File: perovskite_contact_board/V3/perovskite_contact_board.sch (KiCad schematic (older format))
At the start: 39 parts, among them U1 Perovskite_CP_6_Cell, U2 Perovskite_CP_6_Cell, U3 Perovskite_CP_6_Cell, U4 MCP9808_MSOP, U5 MCP9808_MSOP, U6 MCP9808_MSOP

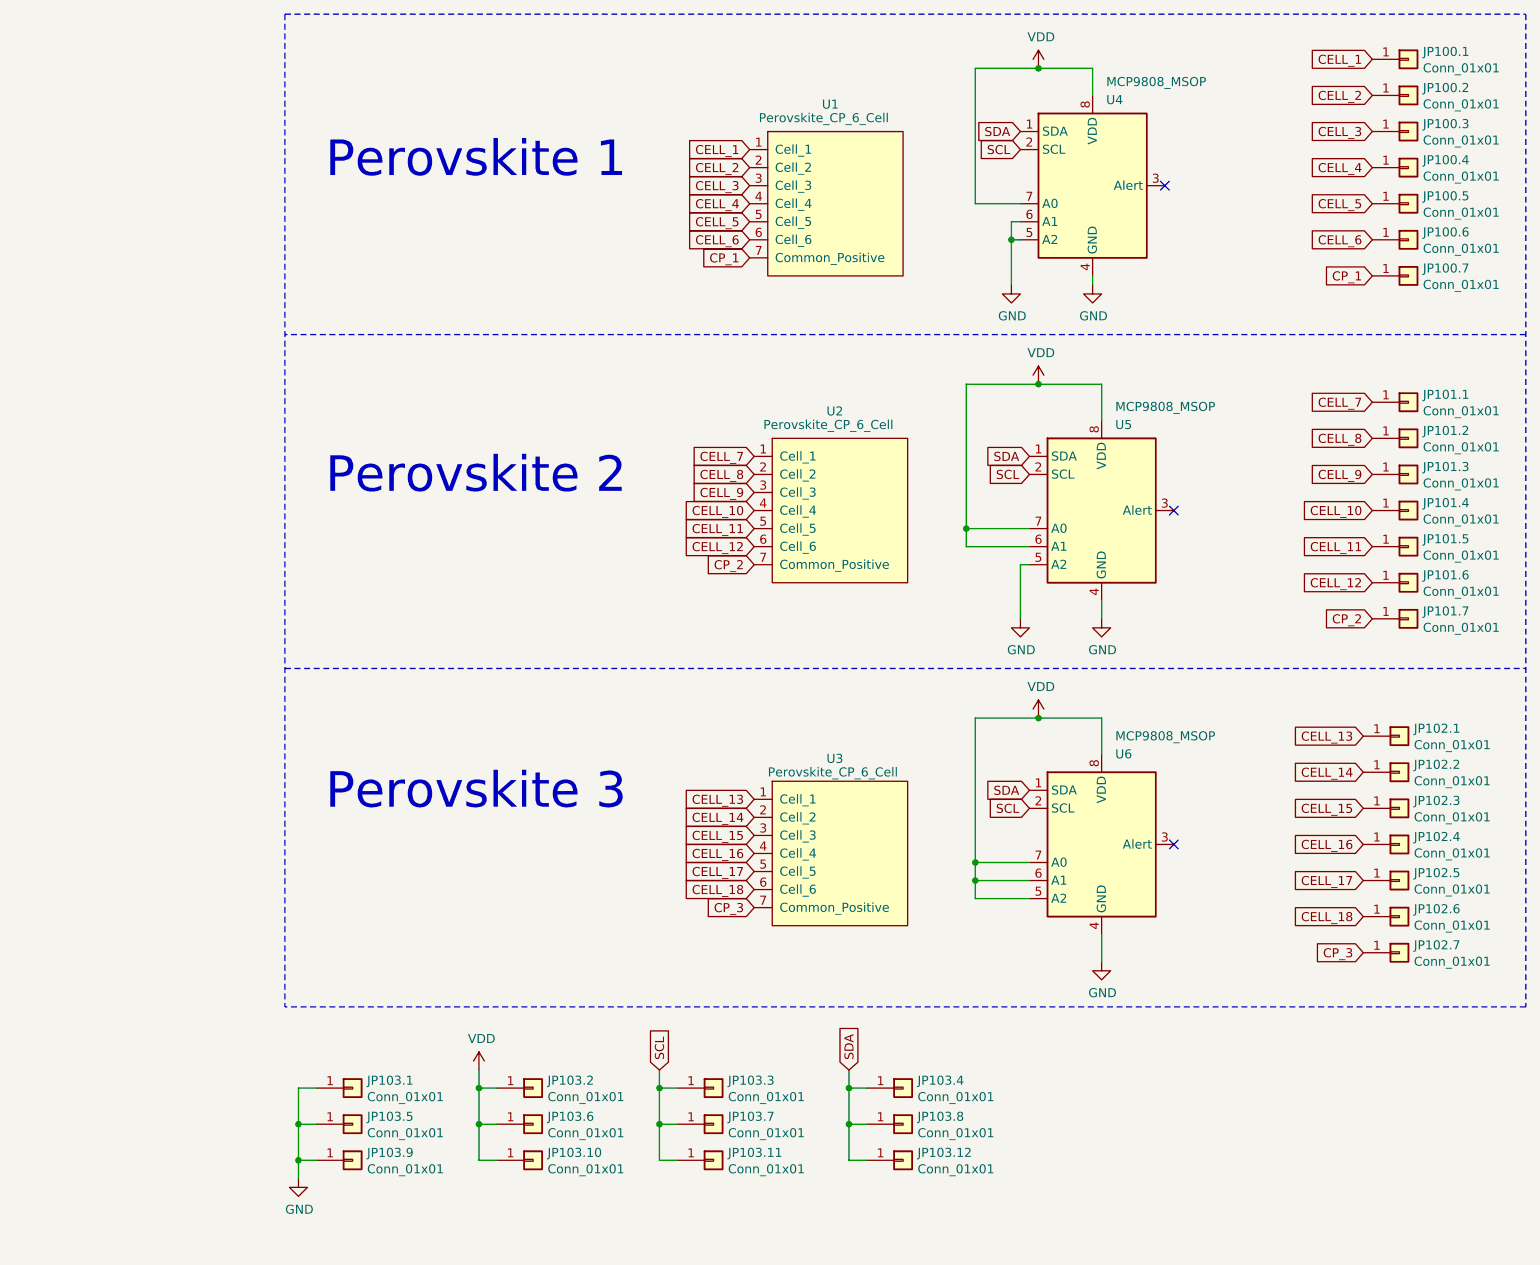
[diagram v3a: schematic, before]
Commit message: isolating nets and fixing silk screen
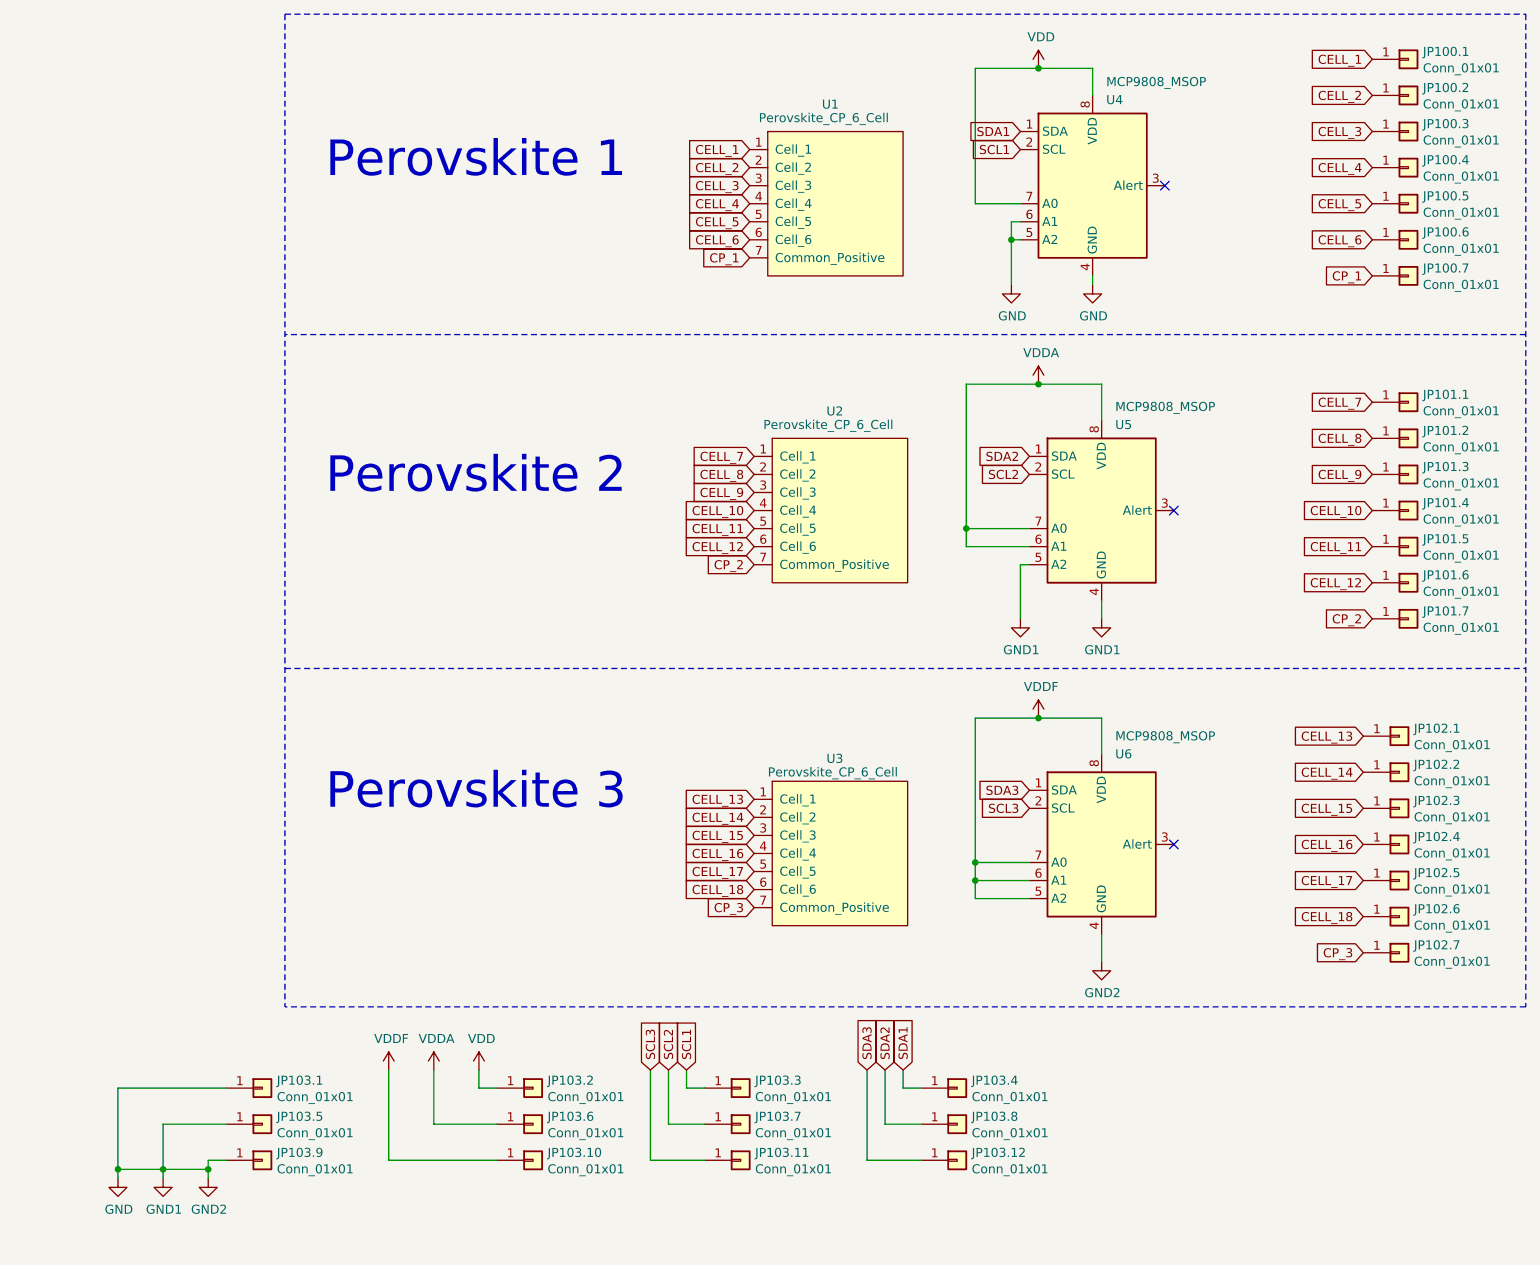
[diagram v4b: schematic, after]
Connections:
- net VDD: no longer JP103.10.1 (Pin_1), JP103.6.1 (Pin_1), U5.6 (A1), U5.7 (A0), U5.8 (VDD), U6.5 (A2), U6.6 (A1), U6.7 (A0), U6.8 (VDD)
- removed net SCL: JP103.11.1 (Pin_1), JP103.3.1 (Pin_1), JP103.7.1 (Pin_1), U4.2 (SCL), U5.2 (SCL), U6.2 (SCL)
- removed net SDA: JP103.12.1 (Pin_1), JP103.4.1 (Pin_1), JP103.8.1 (Pin_1), U4.1 (SDA), U5.1 (SDA), U6.1 (SDA)
- new net SCL1: JP103.3.1 (Pin_1), U4.2 (SCL)
- new net SCL2: JP103.7.1 (Pin_1), U5.2 (SCL)
- new net SCL3: JP103.11.1 (Pin_1), U6.2 (SCL)
- new net SDA1: JP103.4.1 (Pin_1), U4.1 (SDA)
- new net SDA2: JP103.8.1 (Pin_1), U5.1 (SDA)
- new net SDA3: JP103.12.1 (Pin_1), U6.1 (SDA)
- new net VDDA: JP103.6.1 (Pin_1), U5.6 (A1), U5.7 (A0), U5.8 (VDD)
- new net VDDF: JP103.10.1 (Pin_1), U6.5 (A2), U6.6 (A1), U6.7 (A0), U6.8 (VDD)
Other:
- moved on the sheet: JP103.1, JP103.11, JP103.12, JP103.3, JP103.4, JP103.5, JP103.7, JP103.8, JP103.9
